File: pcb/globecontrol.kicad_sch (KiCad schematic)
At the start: 11 parts, among them J1 SLIPRING, J2 HOME, J3 SERVO, J4 LASER, Q1 MMBT2222A, U1 AMS1117-3.3

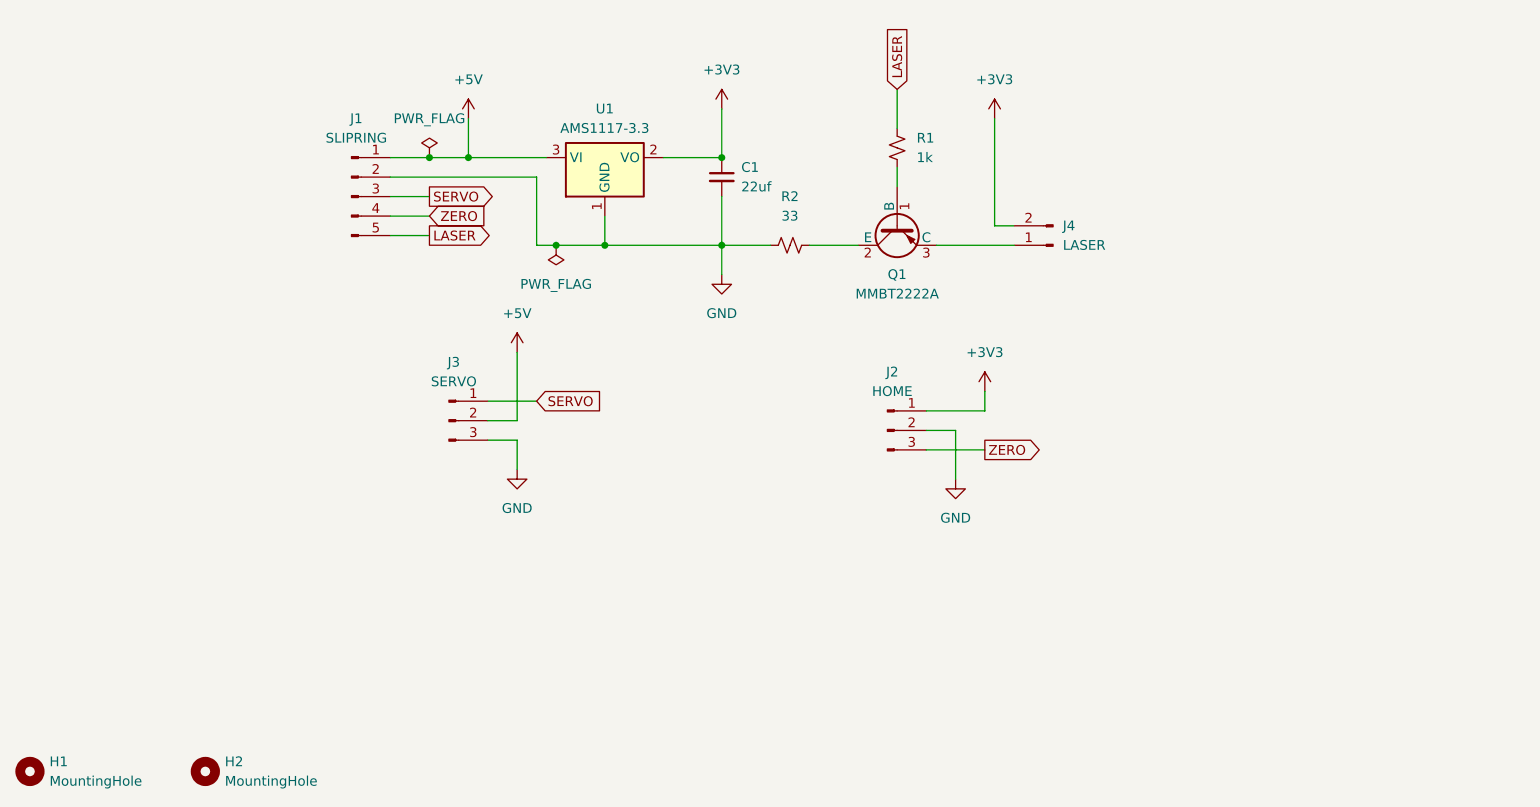
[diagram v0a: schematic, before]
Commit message: Added control for an LED for internal illumination
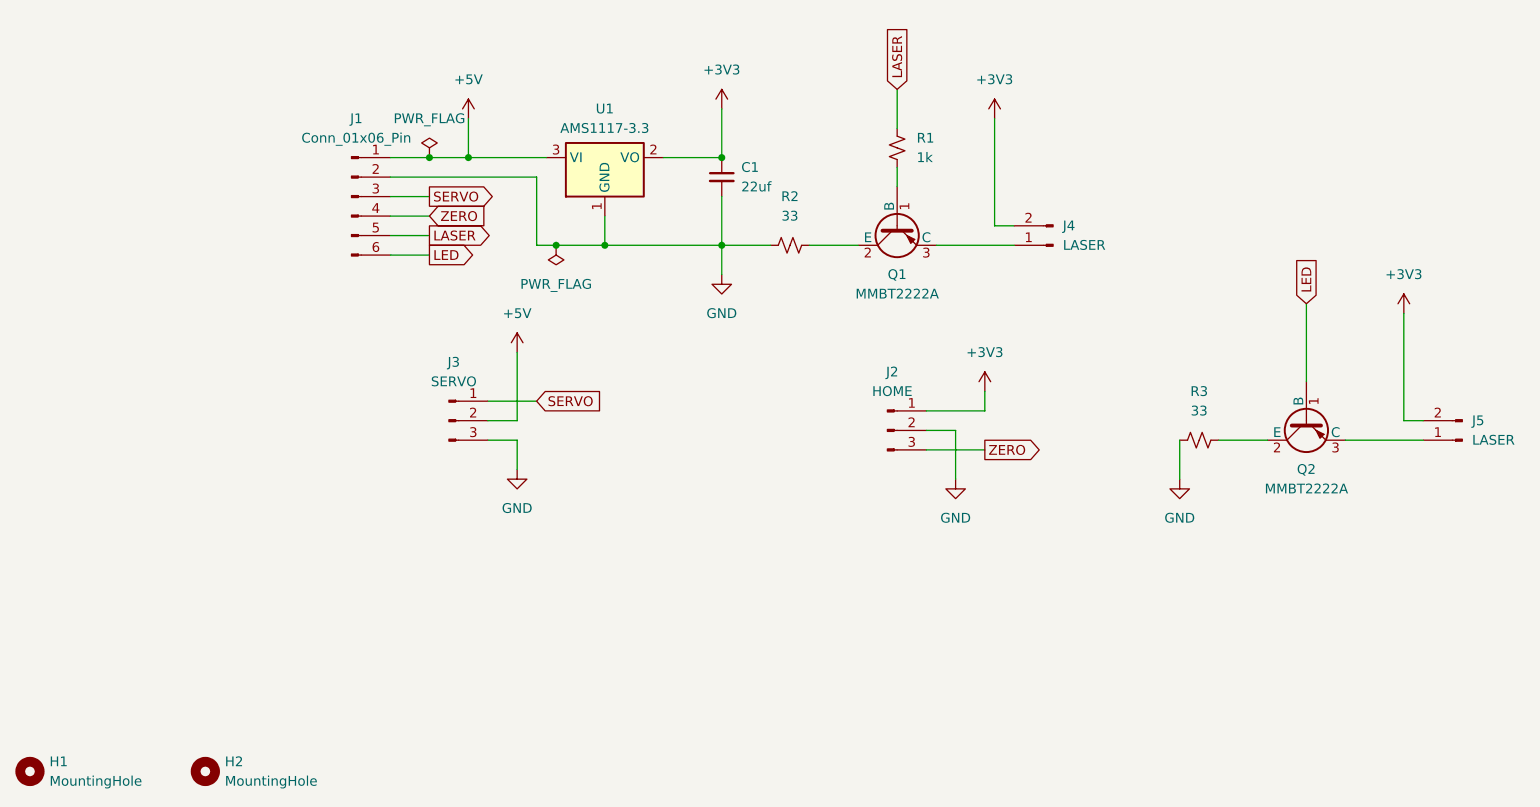
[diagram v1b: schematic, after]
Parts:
- removed J1: SLIPRING, Connector_PinHeader_2.54mm:PinHeader_1x05_P2.54mm_Vertical, symbol Connector:Conn_01x05_Pin
- added J1: Conn_01x06_Pin, Connector_PinHeader_2.54mm:PinHeader_1x06_P2.54mm_Vertical, symbol Connector:Conn_01x06_Pin
- added J5: LASER, Connector_PinHeader_2.54mm:PinHeader_1x02_P2.54mm_Vertical, symbol Connector:Conn_01x02_Pin
- added Q2: MMBT2222A, Package_TO_SOT_SMD:SOT-23, symbol personal:S8550
- added R3: 33, Resistor_SMD:R_0603_1608Metric, symbol Device:R_Small_US
- Q1: LCSC C8512 -> C8550
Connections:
- net +3V3: now also J5.2 (Pin_2)
- net +5V: now also J1.1 (Pin_1)
- net GND: now also J1.2 (Pin_2), R3.1
- net LASER: now also J1.5 (Pin_5)
- net SERVO: now also J1.3 (Pin_3)
- net ZERO: now also J1.4 (Pin_4)
- new net: Q2.2 (E), R3.2
- new net: J5.1 (Pin_1), Q2.3 (C)
- new net LED: J1.6 (Pin_6), Q2.1 (B)
